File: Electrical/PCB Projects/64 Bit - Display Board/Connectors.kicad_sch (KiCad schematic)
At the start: 16 parts, among them J1 Conn_01x03, J2 Conn_01x03, P1 610110249121, P2 610110249121, P3 610110249121

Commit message: slight changes
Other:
- moved on the sheet: D1, D2, D3, D4, D5, D6

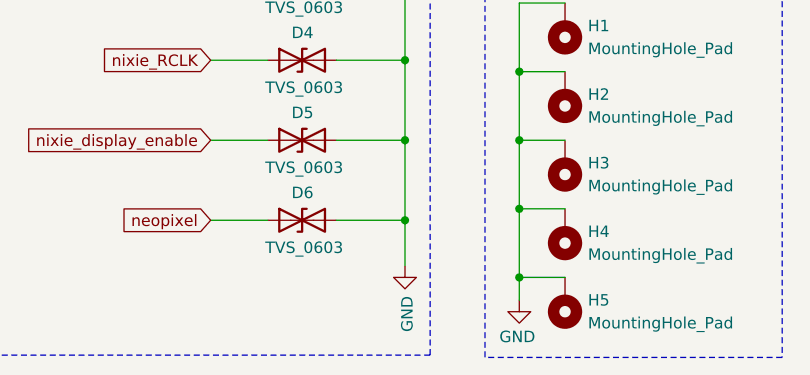
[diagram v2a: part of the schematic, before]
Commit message: final. PCB outputs generated, ordering prototypes
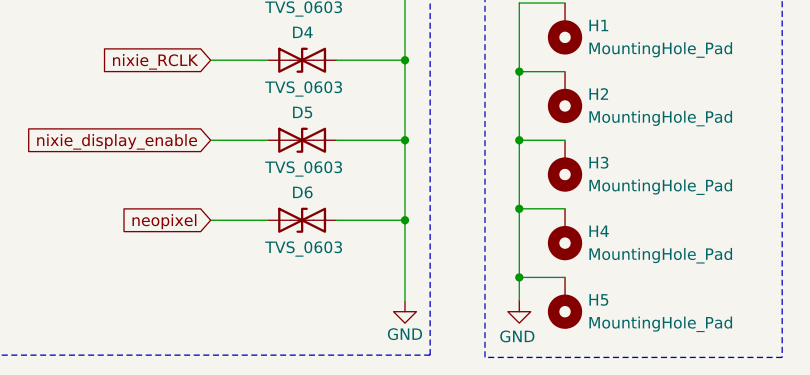
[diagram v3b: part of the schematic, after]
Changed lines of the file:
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@@
 	(wire
 		(pts
-			(xy 115.57 147.32) (xy 115.57 152.4)
+			(xy 115.57 147.32) (xy 115.57 156.21)
 		)
 		(stroke
@@
 	(symbol
 		(lib_id "power:GND")
-		(at 115.57 152.4 0)
+		(at 115.57 156.21 0)
 		(unit 1)
 		(exclude_from_sim no)
@@
 		(dnp no)
 		(property "Reference" "#PWR0150"
-			(at 115.57 158.75 0)
+			(at 115.57 162.56 0)
 			(effects
 				(font
@@
 		)
 		(property "Value" "GND"
-			(at 115.824 157.734 90)
+			(at 115.57 160.02 0)
 			(effects
 				(font
@@
 		)
 		(property "Footprint" ""
-			(at 115.57 152.4 0)
+			(at 115.57 156.21 0)
 			(effects
 				(font
@@
 		)
 		(property "Datasheet" ""
-			(at 115.57 152.4 0)
+			(at 115.57 156.21 0)
 			(effects
 				(font
@@
 		)
 		(property "Description" ""
-			(at 115.57 152.4 0)
-			(effects
-				(font
+			(at 115.57 156.21 0)
+			(effects
+				(font
